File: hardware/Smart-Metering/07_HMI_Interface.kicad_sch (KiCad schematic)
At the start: 0 parts

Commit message: Completa o esquemático: MCU, interface HMI e comunicações
05_Metrology_MCU: STM32F413RHT6 (símbolo oficial), mesma família da
plataforma de referência da biblioteca ADSW-PQ-CLS (NUCLEO-F413ZH).
SPI1 isolado para ADE9430/MCP3204, IRQ/DREADY/ZX em EXTI, CF1/CF2 em
timers, USART2 para a HMI, USART3 + DE para RS-485, USB FS, VBAT_SENSE,
estado do carregador, HSE 8 MHz, RTC com LSE 32,768 kHz e CR2032, SWD
de 10 pinos e LEDs de status e pulso.

07_HMI_Interface: conector J701 para a placa HMI (ESP32-P4), com +5V
protegido por PTC e UART/IRQ/EN com resistores de 33 Ω.

08_Communications: RS-485/Modbus isolada com ADM2587E (terminação por
jumper e TVS) e USB-C de serviço com CC de 5,1 kΩ, ESD USBLC6-2SC6 e
detecção de VBUS.

Gerador: direção dos labels pela orientação do pino, pinos empilhados
tratados como um ponto, flags de não conectado.
README e ARCHITECTURE atualizados com o estado completo.

Co-Authored-By: Claude Opus 5.5 <noreply@anthropic.com>
Claude-Session: https://claude.ai/code/session_012B8cVkhtjf3eg98UdpNCpf
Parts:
- added C701: 22uF, Capacitor_SMD:C_1206_3216Metric, symbol SmartMetering:C_Vert
- added F701: PTC 2A, Fuse:Fuse_1812_4532Metric, symbol SmartMetering:Fuse
- added J701: HMI_LINK, Connector_PinHeader_2.54mm:PinHeader_2x05_P2.54mm_Vertical, symbol Connector_Generic:Conn_02x05_Odd_Even
- added R701, R702, R703, R704: 33R, Resistor_SMD:R_0603_1608Metric, symbol SmartMetering:R_Vert
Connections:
- new net +5V: F701.1
- new net +5V_HMI: C701.1, F701.2, J701.1 (Pin_1), J701.2 (Pin_2)
- new net GND_SYS: C701.2, J701.10 (Pin_10), J701.3 (Pin_3), J701.4 (Pin_4), J701.9 (Pin_9)
- new net HMI_EN: R704.1
- new net HMI_IRQ: R703.1
- new net HMI_RX: R702.2
- new net HMI_TX: R701.1
- new net LINK_EN: J701.8 (Pin_8), R704.2
- new net LINK_IRQ: J701.7 (Pin_7), R703.2
- new net LINK_RX: J701.6 (Pin_6), R702.1
- new net LINK_TX: J701.5 (Pin_5), R701.2
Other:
- note added: "LIGAÇÃO COM A PLACA HMI (ESP32-P4) A HMI fica em placa separada (REQ-010). Protótipo: Espressif ESP32-P4-Function-EV-Board, que já traz ESP32-P4, ESP32-C6 (Wi-Fi 6/BT 5), Ethernet, microSD, USB e o kit de LCD 7" 1024x600 MIPI-DSI. Com isso Ethernet, Wi-Fi, Bluetooth e microSD do REQ-008/REQ-007 ficam na placa HMI. J701: +5V protegido por F701 (PTC 2 A); UART MCU<->P4 (HMI_TX/HMI_RX, 921600 bps su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"
- company: (none) -> Smart-Metering
- title: (none) -> HMI Interface - link to ESP32-P4 board

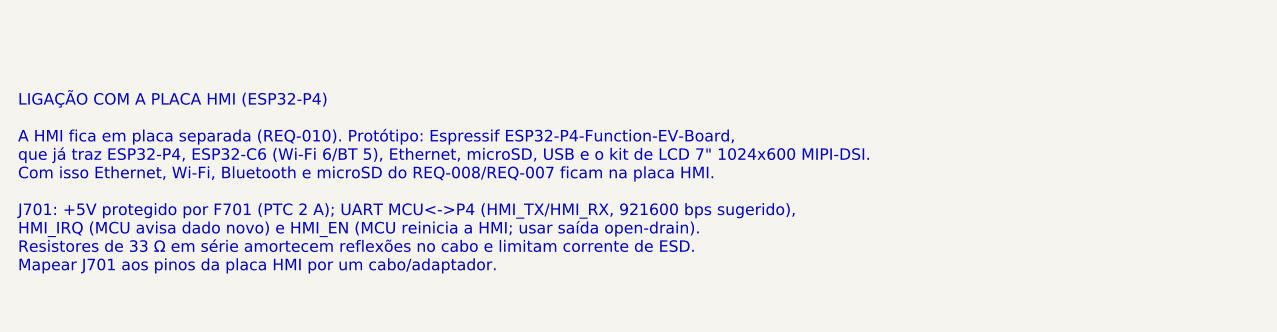
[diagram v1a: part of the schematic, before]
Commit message: Resolve as pendências da revisão do esquemático
P1  ADE9430: footprint VQFN-40 6x6 com EP de 4,15 mm, compatível com as
    variantes CP-40 de 6x6 mm (EP de 3,9 a 4,7 mm).
P2  Confirmado no datasheet: MISO solto com SS alto (pull-up de 100 kΩ)
    e NC1/NC2 em GND, como já estava.
P3  J301-J304: headers JST PH de 4 vias cabeados até conectores M8
    fêmea de painel (à prova de toque).
P4  PS601 -> U606 ADuM6000 (isoPower 5 kVrms, símbolo oficial).
P5  PS101 -> RAC20-05SK/277 (85-305 VAC, 120-430 VDC, 20 W); fusíveis
    T500mA, R101 3 W, C101 10 uF/450 V; entrada do BQ25895 a 3 A.
P7  TPS61089 -> TPS61022 (compensação interna, sem valores a ajustar).
P8  Placa EV alimentada pelos pinos 5 V do J1 (nota na folha 07).
P9  EEPROM de calibração 24LC64 no I2C1.
P10 Labels globais de uma só folha convertidos em locais.

Verificação: 223 componentes, nenhum pino solto, nenhuma net sem fonte,
nenhum conflito de saída, isolação íntegra, todos os footprints
existentes na biblioteca oficial do KiCad.

Co-Authored-By: Claude Opus 5.5 <noreply@anthropic.com>
Claude-Session: https://claude.ai/code/session_012B8cVkhtjf3eg98UdpNCpf
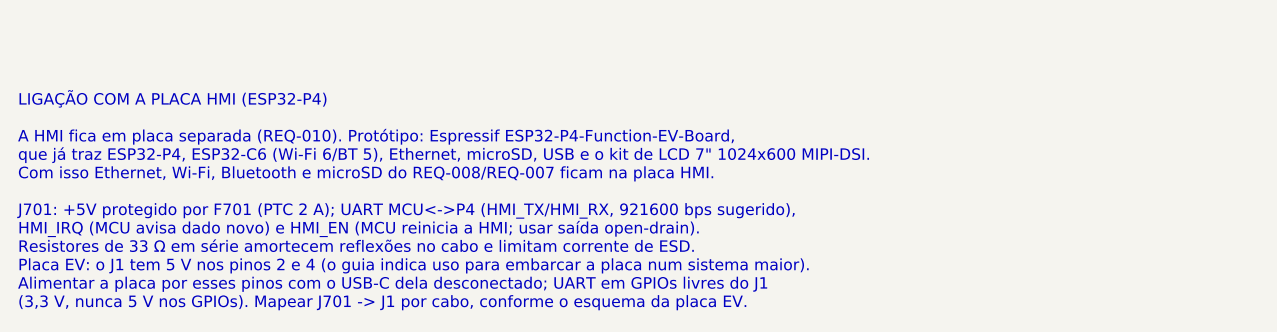
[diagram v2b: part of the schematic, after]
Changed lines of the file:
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@@
 		(comment 2 "Prototype HMI: Espressif ESP32-P4-Function-EV-Board (Ethernet, Wi-Fi/BT, microSD on that board)")
 	)
-	(text "LIGAÇÃO COM A PLACA HMI (ESP32-P4)\n\nA HMI fica em placa separada (REQ-010). Protótipo: Espressif ESP32-P4-Function-EV-Board,\nque já traz ESP32-P4, ESP32-C6 (Wi-Fi 6/BT 5), Ethernet, microSD, USB e o kit de LCD 7\" 1024x600 MIPI-DSI.\nCom isso Ethernet, Wi-Fi, Bluetooth e microSD do REQ-008/REQ-007 ficam na placa HMI.\n\nJ701: +5V protegido por F701 (PTC 2 A); UART MCU<->P4 (HMI_TX/HMI_RX, 921600 bps sugerido),\nHMI_IRQ (MCU avisa dado novo) e HMI_EN (MCU reinicia a HMI; usar saída open-drain).\nResistores de 33 Ω em série amortecem reflexões no cabo e limitam corrente de ESD.\nMapear J701 aos pinos da placa HMI por um cabo/adaptador."
+	(text "LIGAÇÃO COM A PLACA HMI (ESP32-P4)\n\nA HMI fica em placa separada (REQ-010). Protótipo: Espressif ESP32-P4-Function-EV-Board,\nque já traz ESP32-P4, ESP32-C6 (Wi-Fi 6/BT 5), Ethernet, microSD, USB e o kit de LCD 7\" 1024x600 MIPI-DSI.\nCom isso Ethernet, Wi-Fi, Bluetooth e microSD do REQ-008/REQ-007 ficam na placa HMI.\n\nJ701: +5V protegido por F701 (PTC 2 A); UART MCU<->P4 (HMI_TX/HMI_RX, 921600 bps sugerido),\nHMI_IRQ (MCU avisa dado novo) e HMI_EN (MCU reinicia a HMI; usar saída open-drain).\nResistores de 33 Ω em série amortecem reflexões no cabo e limitam corrente de ESD.\nPlaca EV: o J1 tem 5 V nos pinos 2 e 4 (o guia indica uso para embarcar a placa num sistema maior).\nAlimentar a placa por esses pinos com o USB-C dela desconectado; UART em GPIOs livres do J1\n(3,3 V, nunca 5 V nos GPIOs). Mapear J701 -> J1 por cabo, conforme o esquema da placa EV."
 		(exclude_from_sim no)(at 25.4 152.4 0)
 		(effects (font (size 1.27 1.27)) (justify left top))
